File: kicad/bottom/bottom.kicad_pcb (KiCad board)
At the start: 2 copper layers, 65 x 120 mm, 17 parts, among them J1 Conn_01x15_Socket

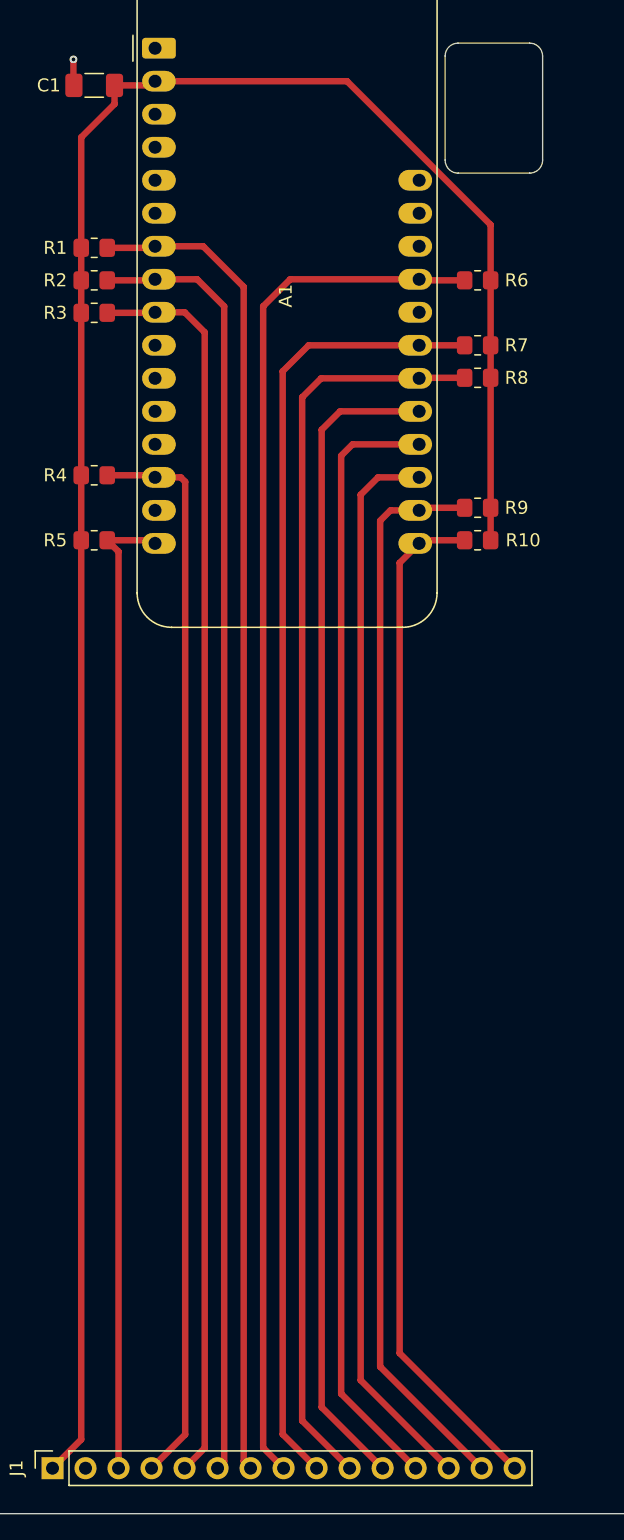
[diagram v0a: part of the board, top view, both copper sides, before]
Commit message: added teardrops to every pad, removed the raw images from repo
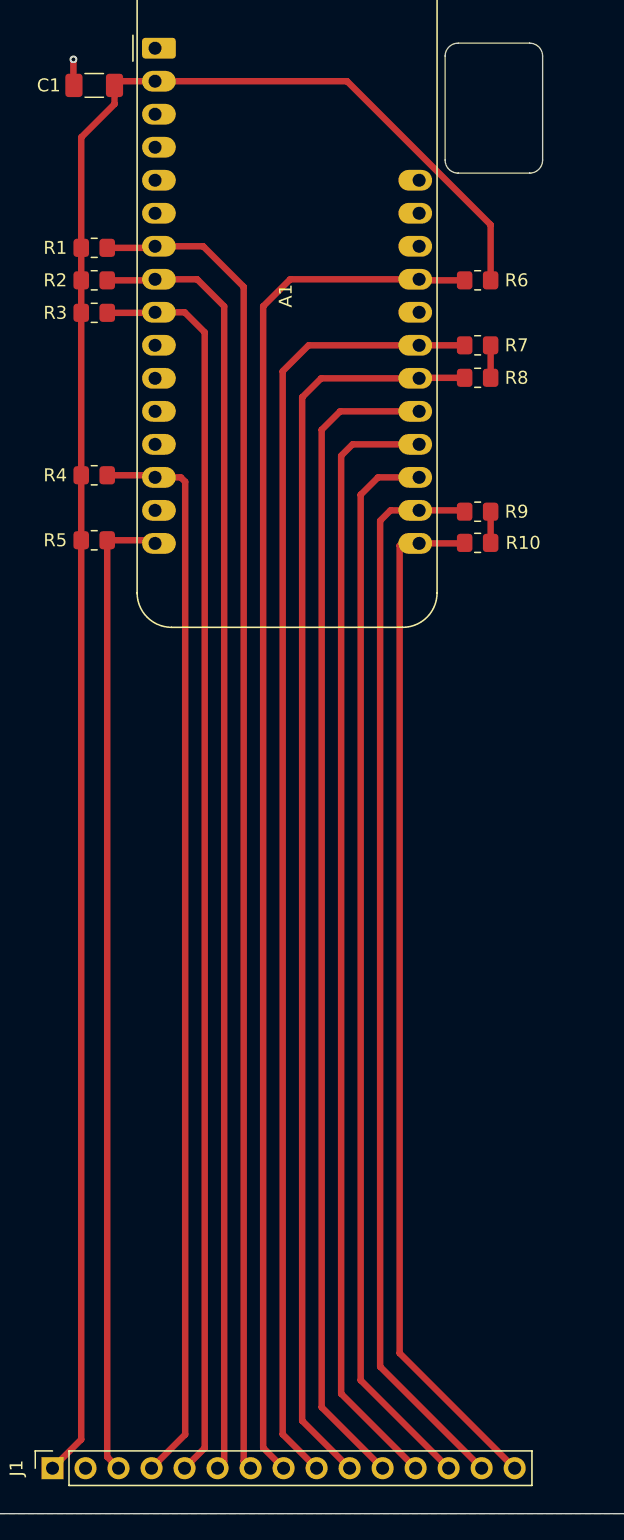
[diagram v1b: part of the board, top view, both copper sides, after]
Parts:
- moved R9 0.30 mm to (63.0, 58.8)
- moved R10 0.20 mm to (63.0, 61.2)
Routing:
- net +3.3V: track 166.3 -> 151.2 mm
- net OLED_SDA: track 79.0 -> 79.7 mm

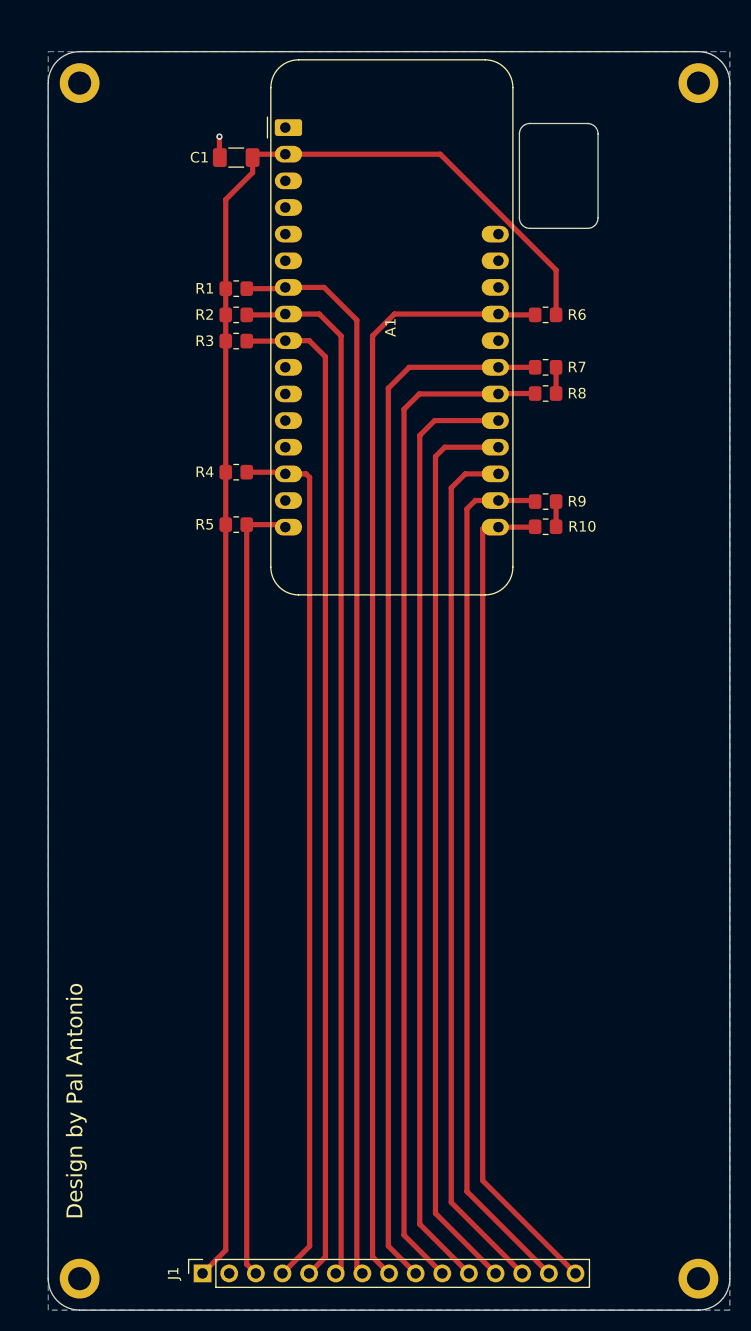
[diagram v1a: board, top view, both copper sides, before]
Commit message: Changed from Adafruit Feather V2 to UnkownMaker ProS3 [D] for USB HID feature. Changed OLED from 128x64 to 128x32
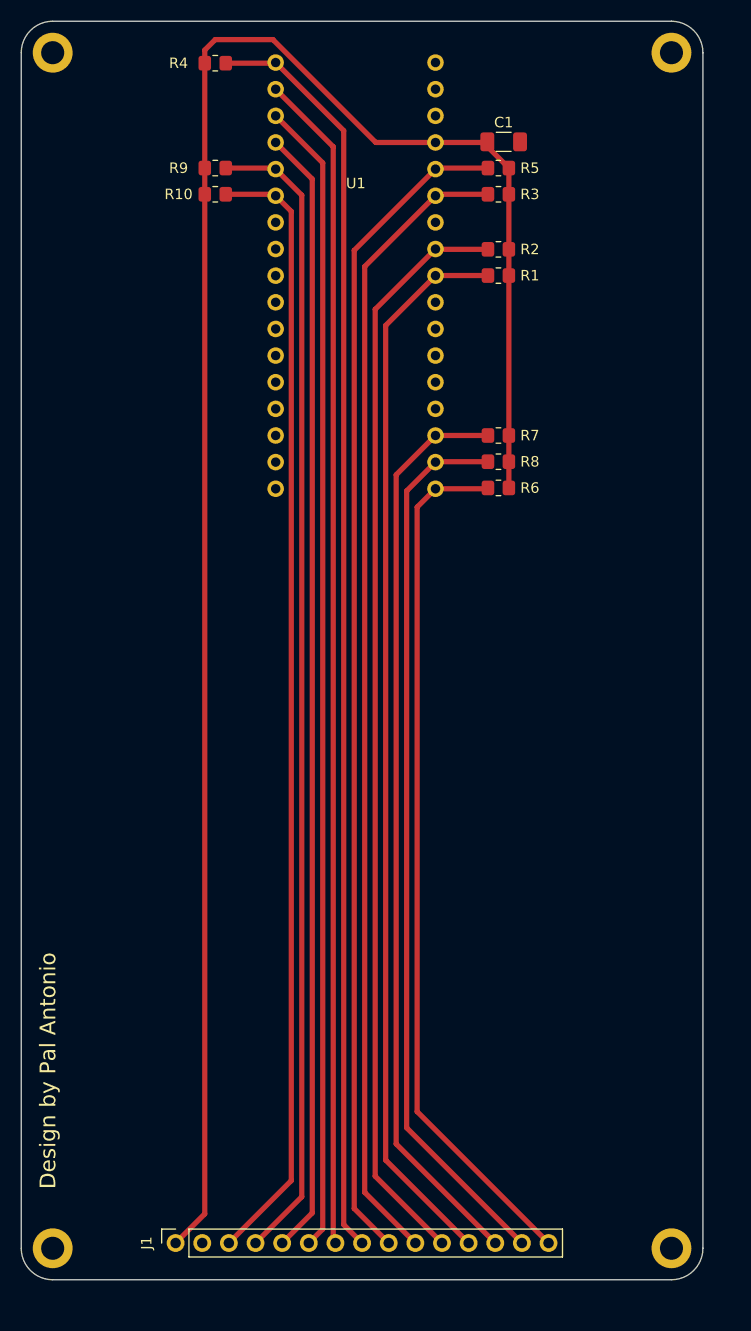
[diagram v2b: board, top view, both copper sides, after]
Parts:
- removed A1: Adafruit_Feather_V2, Bottom-Footprints:Adafruit_Feather
- added U1: ~, Bottom-Footprints:ProS3_TH, F.Cu at (44.9, 37.3)
- moved R9 44.8 mm to (31.5, 27.0), turned to 0 degrees
- moved R10 44.7 mm to (31.5, 29.5), turned to 0 degrees
- moved R5 42.2 mm to (58.5, 27.0), turned to 180 degrees
- moved R4 39.1 mm to (31.5, 17.0)
- moved R3 28.7 mm to (58.5, 29.5), turned to 180 degrees
- moved R2 25.8 mm to (58.5, 34.8), turned to 180 degrees
- moved C1 25.5 mm to (59.0, 24.5), turned to 0 degrees
- moved R1 25.0 mm to (58.5, 37.2), turned to 180 degrees
- moved R6 17.1 mm to (58.5, 57.5)
- moved R7 7.91 mm to (58.5, 52.5)
- moved R8 7.91 mm to (58.5, 55.0)
- moved H4 3.87 mm to (16.0, 130.0)
- moved J1 3.87 mm to (27.7, 129.5)
- moved H3 3.87 mm to (75.0, 130.0)
- moved H1 3.87 mm to (16.0, 16.0)
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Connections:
- J1 pad 10: ENC_SW -> ROW2
- J1 pad 11: COL0 -> ROW1
- J1 pad 12: COL1 -> ROW0
- J1 pad 13: COL2 -> ENC_DT
- J1 pad 14: OLED_SCL -> ENC_SW
- J1 pad 15: OLED_SDA -> ENC_CLK
- J1 pad 3: ROW3 -> OLED_SDA
- J1 pad 4: BT_SELECT -> OLED_SCL
- J1 pad 5: ROW2 -> COL0
- J1 pad 6: ROW1 -> COL1
- J1 pad 7: ROW0 -> COL2
- J1 pad 8: ENC_CLK -> BT_SELECT
- J1 pad 9: ENC_DT -> ROW3
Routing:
- net BT_SELECT: track 83.2 -> 120.7 mm
- net ROW3: track 75.5 -> 111.5 mm
- net COL2: track 82.8 -> 112.1 mm
- net +3.3V: track 151.2 -> 179.7 mm
- net OLED_SDA: track 79.7 -> 107.6 mm
- net OLED_SCL: track 83.0 -> 109.9 mm
- net ENC_CLK: track 106.4 -> 82.5 mm
- net COL1: track 86.6 -> 109.9 mm
- net COL0: track 89.9 -> 107.6 mm
- net ROW2: track 96.2 -> 109.5 mm
- net ENC_DT: track 100.3 -> 87.5 mm
- net ENC_SW: track 97.0 -> 85.2 mm
- net ROW1: track 99.5 -> 104.8 mm
- net GND: track 2.02 -> 0.00 mm, vias 1 -> 0
- removed copper zone on B.Cu, net GND
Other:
- outline, holes or cut-outs redrawn

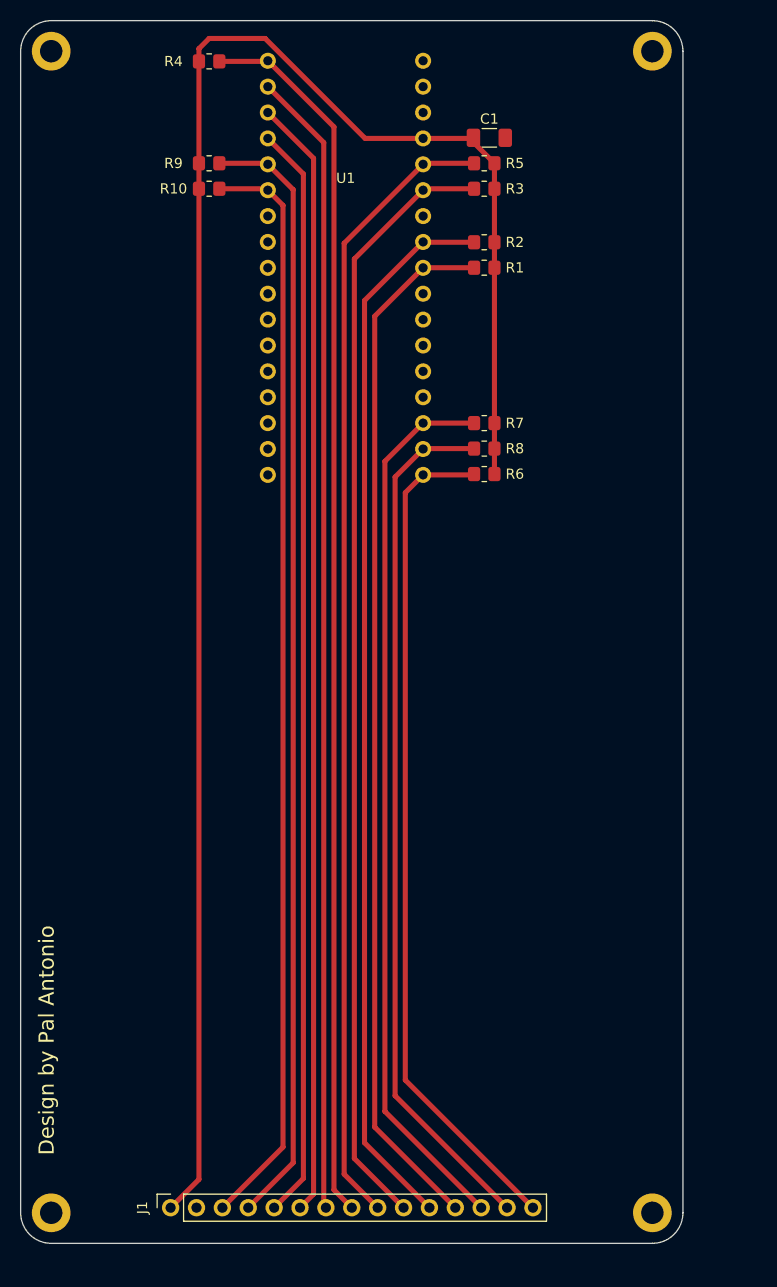
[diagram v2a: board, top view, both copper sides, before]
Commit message: added visuals, updated the documentation
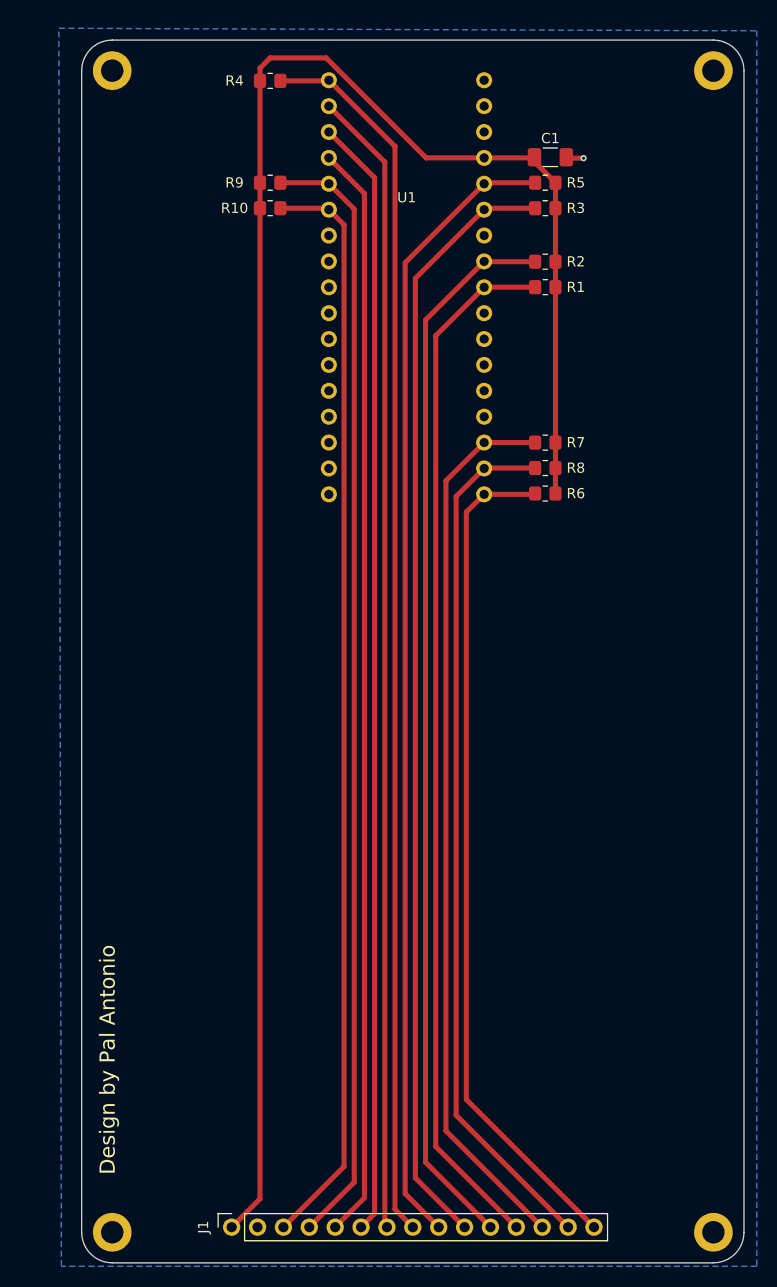
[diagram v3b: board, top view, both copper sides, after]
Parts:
- moved U1 6.29 mm to (50.9, 39.2)
- moved J1 6.29 mm to (33.7, 131.4)
- moved R10 6.29 mm to (37.5, 31.4)
- moved R4 6.29 mm to (37.5, 18.9)
- moved R9 6.29 mm to (37.5, 28.9)
- moved H1 6.29 mm to (22.0, 17.9)
- moved H4 6.29 mm to (22.0, 131.9)
- moved C1 6.29 mm to (65.0, 26.4)
- moved H2 6.29 mm to (81.0, 17.9)
- moved R3 6.29 mm to (64.5, 31.4)
- moved R5 6.29 mm to (64.5, 28.9)
- moved H3 6.29 mm to (81.0, 131.9)
- moved R1 6.29 mm to (64.5, 39.2)
- moved R2 6.29 mm to (64.5, 36.7)
- moved R6 6.29 mm to (64.5, 59.4)
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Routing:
- net GND: track 0.00 -> 1.73 mm, vias 0 -> 1
- added copper zone on B.Cu, net GND
